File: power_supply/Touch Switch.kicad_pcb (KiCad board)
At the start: 2 copper layers, 82.9 x 49.8 mm, 51 parts, among them J1 Conn_01x01_Pin, J2 Conn_02x04_Counter_Clockwise, J3 Conn_01x01_Pin, J4 Conn_01x01_Pin, J5 Conn_01x01_Pin, J6 Conn_01x01_Pin, J7 Conn_01x01_Pin, J8 Conn_01x01_Pin, K1 Relay_SPST-NO, K2 Relay_SPST-NO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

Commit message: Modification : PCB
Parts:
- added G***: LOGO, LOGO, F.Cu at (191.8, 108.2)
- moved K2 8.88 mm to (191.2, 83.4)
- moved K4 8.78 mm to (204.9, 83.4)
- moved K3 8.77 mm to (177.6, 83.4)
- moved K1 8.72 mm to (218.5, 83.4)
- moved C6 1.45 mm to (150.4, 72.3), turned to 90 degrees
- moved D6 0.51 mm to (198.6, 77.9)
- moved Q1 0.51 mm to (194.9, 78.7)
- moved R12 0.51 mm to (191.8, 78.7)
- moved D5 0.35 mm to (225.9, 78.2)
- moved D7 0.10 mm to (212.7, 78.2)
- moved Q3 0.10 mm to (209.1, 79.0)
- moved R14 0.10 mm to (205.9, 79.0)
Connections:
- K1 pad 13: L -> R1
- K1 pad 14: R1 -> L
- K2 pad 13: L -> R3
- K2 pad 14: R3 -> L
- K3 pad 13: L -> R4
- K3 pad 14: R4 -> L
- K4 pad 13: L -> R2
- K4 pad 14: R2 -> L
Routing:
- net L: track 126.7 -> 0.00 mm, vias 46 -> 50
- net GND2: track 103.0 -> 199.2 mm, vias 4 -> 3
- net R1: track 23.7 -> 2.21 mm
- net R3: track 23.8 -> 2.28 mm
- net R2: track 23.8 -> 2.76 mm
- net R4: track 19.5 -> 0.01 mm
- net GND: track 59.2 -> 78.3 mm
- net N: track 23.2 -> 15.5 mm, vias 4 -> 6
- net Net-(D9-+): track 14.6 -> 21.0 mm, vias 0 -> 1
- net +5V: track 168.0 -> 163.3 mm
- net VCC_IC: track 8.73 -> 9.82 mm
- net Net-(D5-A): track 14.1 -> 13.1 mm
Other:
- board size 82.9 x 49.8 mm -> 82.9 x 50 mm

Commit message: Modified : PCB
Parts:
- moved R5 0.17 mm to (151.7, 69.8)
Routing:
- net Net-(S713XS1-FB): track 9.11 -> 3.58 mm, vias 2 -> 4
- net Prim: track 16.7 -> 11.5 mm, vias 3 -> 4
- net GND2: track 199.2 -> 195.7 mm, vias 3 -> 6
- net Net-(D9-+): track 21.0 -> 22.2 mm, vias 1 -> 2
- net GND: track 78.3 -> 79.1 mm, vias 3 -> 6

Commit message: Modified : PCB
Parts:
- moved R5 0.21 mm to (151.7, 69.5)
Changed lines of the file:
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@@
 	(footprint "Resistor_SMD:R_0805_2012Metric"
 		(layer "F.Cu")
-		(at 151.65 69.7625 180)
+		(at 151.65 69.55 180)
 		(descr "Resistor SMD 0805 (2012 Metric), square (rectangular) end terminal, IPC_7351 nominal, (Body size source: IPC-SM-782 page 72, https://www.pcb-3d.com/wordpress/wp-content/uploads/ipc-sm-782a_amendment_1_and_2.pdf), generated with kicad-footprint-generator")
 		(tags "resistor")
@@
 		(at 159.75 81.55)
 		(size 1)
-		(drill 0.25)
+		(drill 0.3)
 		(layers "F.Cu" "B.Cu")
 		(net 9)

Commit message: New Kicad Project + tree modified
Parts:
- moved R1 1.12 mm to (156.7, 95.1)
- moved L1 0.96 mm to (150.8, 97.1)
- moved C7 0.75 mm to (158.1, 102.2)
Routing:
- net GND: track 79.1 -> 83.3 mm
- net 310VDC: track 53.9 -> 56.1 mm
- net Net-(S713XS1-CS): track 1.93 -> 0.00 mm
- net Net-(C7-Pad1): track 7.92 -> 9.29 mm
- net Net-(D9-+): track 22.2 -> 23.6 mm
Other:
- board size 82.9 x 50 mm -> 84.5 x 50 mm

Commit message: PCB (control_card): Almost Finished
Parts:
- moved J2 5.21 mm to (220.9, 67.9)
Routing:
- net CT3: track 35.6 -> 30.8 mm
- net CT1: track 46.4 -> 41.8 mm
- net GND2: track 195.7 -> 192.1 mm
- net +3.3V: track 28.5 -> 24.9 mm
- net CT4: track 29.2 -> 27.5 mm
- net CT2: track 23.8 -> 22.5 mm
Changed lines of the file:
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@@
 	(footprint "Connector_PinSocket_2.54mm:PinSocket_2x04_P2.54mm_Vertical"
 		(layer "F.Cu")
-		(at 225.5 70.29 -90)
+		(at 220.895183 67.85825 -90)
 		(descr "Through hole straight socket strip, 2x04, 2.54mm pitch, double cols (from Kicad 4.0.7), script generated")
 		(tags "Through hole socket strip THT 2x04 2.54mm double row")
@@
 		(net 16)
 	)
+	(gr_line
+		(start 173.99 63.25)
+		(end 173.99 88.19)
+		(stroke
+			(width 0.1)
+			(type default)
+		)
+		(layer "Dwgs.User")
+	)
+	(gr_line
+		(start 173.99 88.19)
+		(end 229.58 88.19)
+		(stroke
+			(width 0.1)
+			(type default)
+		)
+		(layer "Dwgs.User")
+	)
 	(gr_arc
 		(start 173 80.5)
@@
 			(extension_offset 0.5) keep_text_aligned)
 	)
+	(dimension
+		(type aligned)
+		(layer "F.SilkS")
+		(pts
+			(xy 222.225183 63.98825) (xy 229.52 63.98)
+		)
+		(height -7.104325)
+		(gr_text "7,2948 mm"
+			(at 225.863313 55.779806 0.06479804972)
+			(layer "F.SilkS")
+			(effects
+				(font
+					(size 1 1)
+					(thickness 0.1)
+				)
+			)
+		)
+		(format
+			(prefix "")
+			(suffix "")
+			(units 3)
+			(units_format 1)
+			(precision 4)
+		)
+		(style
+			(thickness 0.1)
+			(arrow_length 1.27)
+			(text_position_mode 0)
+			(extension_height 0.58642)
+			(extension_offset 0.5) keep_text_aligned)
+	)
+	(dimension
+		(type aligned)
+		(layer "Dwgs.User")
+		(pts
+			(xy 173.99 63.25) (xy 229.52 63.25)
+		)
+		(height -13.01)
+		(gr_text "55,5300 mm"
+			(at 201.755 49.09 0)
+			(layer "Dwgs.User")
+			(effects
+				(font
+					(size 1 1)
+					(thickness 0.15)
+				)
+			)
+		)
+		(format
+			(prefix "")
+			(suffix "")
+			(units 3)
+			(units_format 1)
+			(precision 4)
+		)
+		(style
+			(thickness 0.1)
+			(arrow_length 1.27)
+			(text_position_mode 0)
+			(extension_height 0.58642)
+			(extension_offset 0.5) keep_text_aligned)
+	)
+	(dimension
+		(type aligned)
+		(layer "Dwgs.User")
+		(pts
+			(xy 229.52 63.25) (xy 229.58 88.19)
+		)
+		(height -16.153435)
+		(gr_text "24,9401 mm"
+			(at 246.853385 75.678372 270.1378404)
+			(layer "Dwgs.User")
+			(effects
+				(font
+					(size 1 1)
+					(thickness 0.15)
+				)
+			)
+		)
+		(format
+			(prefix "")
+			(suffix "")
+			(units 3)
+			(units_format 1)
+			(precision 4)
+		)
+		(style
+			(thickness 0.1)
+			(arrow_length 1.27)
+			(text_position_mode 0)
+			(extension_height 0.58642)
+			(extension_offset 0.5) keep_text_aligned)
+	)
 	(segment
 		(start 150.7 69.8)
@@
 	)
 	(segment
-		(start 205.925 77.9875)
-		(end 208.1375 77.9875)
+		(start 208.175 76.925)
+		(end 209.75 75.35)
 		(width 0.2)
 		(layer "F.Cu")
@@
 	)
 	(segment
-		(start 227 68.5)
-		(end 226.25 67.75)
+		(start 223.28 69.16)
+		(end 223.28 65.94)
 		(width 0.2)
 		(layer "F.Cu")
@@
 	)
 	(segment
-		(start 223.25 75.35)
-		(end 227 71.6)
+		(start 222.65825 65.31825)
+		(end 220.895183 65.31825)
 		(width 0.2)
 		(layer "F.Cu")
@@
 	)
 	(segment
-		(start 208.175 77.95)
-		(end 208.175 76.925)
+		(start 217.09 75.35)
+		(end 223.28 69.16)
 		(width 0.2)
 		(layer "F.Cu")
@@
 	)
 	(segment
-		(start 208.175 76.925)
-		(end 209.75 75.35)
+		(start 208.1375 77.9875)
+		(end 208.175 77.95)
 		(width 0.2)
 		(layer "F.Cu")
@@
 	)
 	(segment
-		(start 227 71.6)
-		(end 227 68.5)
+		(start 209.75 75.35)
+		(end 217.09 75.35)
 		(width 0.2)
 		(layer "F.Cu")
@@
 	)
 	(segment
-		(start 209.75 75.35)
-		(end 223.25 75.35)
+		(start 223.28 65.94)
+		(end 222.65825 65.31825)
 		(width 0.2)
 		(layer "F.Cu")
@@
 	)
 	(segment
-		(start 226.25 67.75)
-		(end 225.5 67.75)
+		(start 208.175 77.95)
+		(end 208.175 76.925)
 		(width 0.2)
 		(layer "F.Cu")
@@
 	)
 	(segment
-		(start 208.1375 77.9875)
-		(end 208.175 77.95)
+		(start 205.925 77.9875)
+		(end 208.1375 77.9875)
 		(width 0.2)
 		(layer "F.Cu")
@@
 	)
 	(segment
-		(start 222.96 72.24)
-		(end 220.45 74.75)
-		(width 0.2)
-		(layer "F.Cu")
-		(net 24)
-	)
-	(segment
-		(start 192.4125 77.8)
-		(end 192.3 77.6875)
+		(start 194.05 76.75)
+		(end 194.05 77.8)
 		(width 0.2)
 		(layer "F.Cu")
@@
 	)
 	(segment
-		(start 194.05 77.8)
-		(end 192.4125 77.8)
+		(start 196.05 74.75)
+		(end 194.05 76.75)
 		(width 0.2)
 		(layer "F.Cu")
@@
 	)
 	(segment
-		(start 220.45 74.75)
-		(end 196.05 74.75)
+		(start 218.355183 67.85825)
+		(end 211.463433 74.75)
 		(width 0.2)
 		(layer "F.Cu")
@@
 	)
 	(segment
-		(start 194.05 76.75)
-		(end 194.05 77.8)
+		(start 194.05 77.8)
+		(end 192.4125 77.8)
 		(width 0.2)
 		(layer "F.Cu")
@@
 	)
 	(segment
-		(start 222.96 70.29)
-		(end 222.96 72.24)
+		(start 192.4125 77.8)
+		(end 192.3 77.6875)
 		(width 0.2)
 		(layer "F.Cu")
@@
 	)
 	(segment
-		(start 196.05 74.75)
-		(end 194.05 76.75)
+		(start 211.463433 74.75)
+		(end 196.05 74.75)
 		(width 0.2)
 		(layer "F.Cu")
@@
 	)
 	(segment
+		(start 210.883433 70.25)
+		(end 213.275183 67.85825)
+		(width 1)
+		(layer "F.Cu")
+		(net 25)
+	)
+	(segment
 		(start 201.7 70.7)
 		(end 206.4375 70.7)
@@
 	)
 	(segment
-		(start 217.84 70.25)
-		(end 217.88 70.29)
-		(width 1)
-		(layer "F.Cu")
-		(net 25)
-	)
-	(segment
 		(start 189.55 78.75)
 		(end 190.3125 79.5125)
@@
 	)
 	(segment
-		(start 209 70.25)
-		(end 217.84 70.25)
-		(width 1)
-		(layer "F.Cu")
-		(net 25)
-	)
-	(segment
 		(start 185.2 70.3)
 		(end 188 73.1)
@@
 		(net 25)
 	)
+	(segment
+		(start 209 70.25)
+		(end 210.883433 70.25)
+		(width 1)
+		(layer "F.Cu")
+		(net 25)
+	)
 	(via
 		(at 189.55 77.95)
@@
 	)
 	(segment
-		(start 227.8 66.2)
-		(end 227.1 65.5)
+		(start 221.425 77.8875)
+		(end 221.4625 77.85)
 		(width 0.2)
 		(layer "F.Cu")
@@
 	)
 	(segment
-		(start 227.1 65.5)
-		(end 223.7 65.5)
+		(start 223.78 64.76)
+		(end 223.78 69.56)
 		(width 0.2)
 		(layer "F.Cu")
@@
 	)
 	(segment
-		(start 221.425 77.8875)
-		(end 221.4625 77.85)
+		(start 219.505183 64.16825)
+		(end 223.18825 64.16825)
 		(width 0.2)
 		(layer "F.Cu")
@@
 	)
 	(segment
-		(start 221.4625 77.85)
-		(end 222.05 77.85)
+		(start 221.4625 71.8775)
+		(end 221.4625 77.85)
 		(width 0.2)
 		(layer "F.Cu")
@@
 	)
 	(segment
-		(start 223.7 65.5)
-		(end 222.96 66.24)
+		(start 223.78 69.56)
+		(end 221.4625 71.8775)
 		(width 0.2)
 		(layer "F.Cu")
@@
 	)
 	(segment
-		(start 227.8 72.1)
-		(end 227.8 66.2)
+		(start 218.355183 65.31825)
+		(end 219.505183 64.16825)
 		(width 0.2)
 		(layer "F.Cu")
@@
 	)
 	(segment
-		(start 222.96 66.24)
-		(end 222.96 67.75)
+		(start 223.18825 64.16825)
+		(end 223.78 64.76)
 		(width 0.2)
 		(layer "F.Cu")
@@
 	)
 	(segment
-		(start 222.05 77.85)
-		(end 227.8 72.1)
-		(width 0.2)
-		(layer "F.Cu")
-		(net 26)
-	)
-	(segment
 		(start 181.125 77.65)
 		(end 181.125 76.0125)
@@
 	)
 	(segment
-		(start 182.9375 74.2)
-		(end 218.2 74.2)
+		(start 209.473433 74.2)
+		(end 215.815183 67.85825)
 		(width 0.2)
 		(layer "F.Cu")
@@
 	)
 	(segment
-		(start 220.42 71.98)
-		(end 220.42 70.29)
-		(width 0.2)
-		(layer "F.Cu")
-		(net 27)
-	)
-	(segment
 		(start 179.15 77.65)
 		(end 179.0625 77.7375)
@@
 	)
 	(segment
-		(start 218.2 74.2)
-		(end 220.42 71.98)
+		(start 182.9375 74.2)
+		(end 209.473433 74.2)
 		(width 0.2)
 		(layer "F.Cu")
@@
 	)
 	(segment
-		(start 217.28 68.35)
-		(end 217.88 67.75)
-		(width 1)
-		(layer "F.Cu")
-		(net 28)
-	)
-	(segment
 		(start 208.4875 67.8375)
 		(end 209 68.35)
@@
 	)
 	(segment
-		(start 209 68.35)
-		(end 217.28 68.35)
-		(width 1)
-		(layer "F.Cu")
-		(net 28)
-	)
-	(segment
 		(start 196.85 69.6)
 		(end 190.55 69.6)
@@
 	)
 	(segment
+		(start 210.243433 68.35)
+		(end 213.275183 65.31825)
+		(width 1)
+		(layer "F.Cu")
+		(net 28)
+	)
+	(segment
 		(start 196.85 69.6)
 		(end 198.7 69.6)
 		(width 1)
 		(layer "F.Cu")
+		(net 28)
+	)
+	(segment
+		(start 209 68.35)
+		(end 210.243433 68.35)
+		(width 1)
+		(layer "F.Cu")

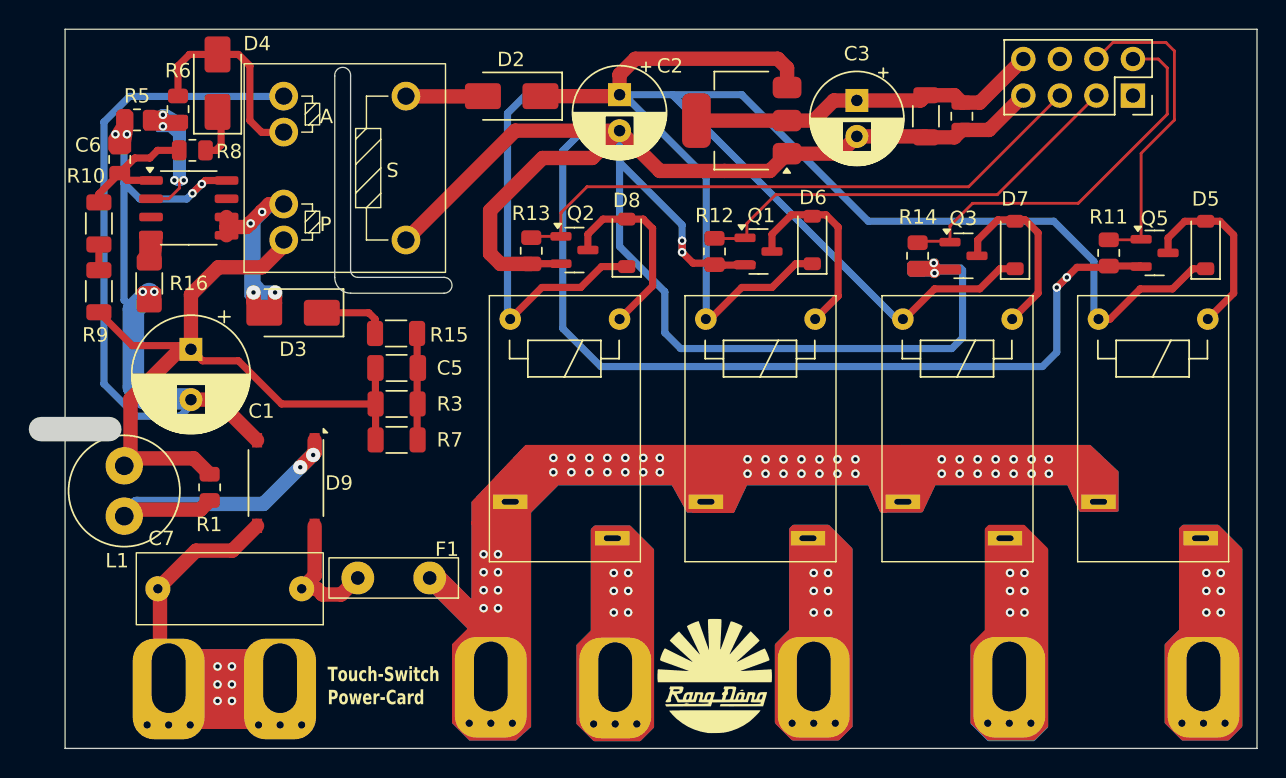
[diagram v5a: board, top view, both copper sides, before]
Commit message: PCB (control_card): V2 almost finished
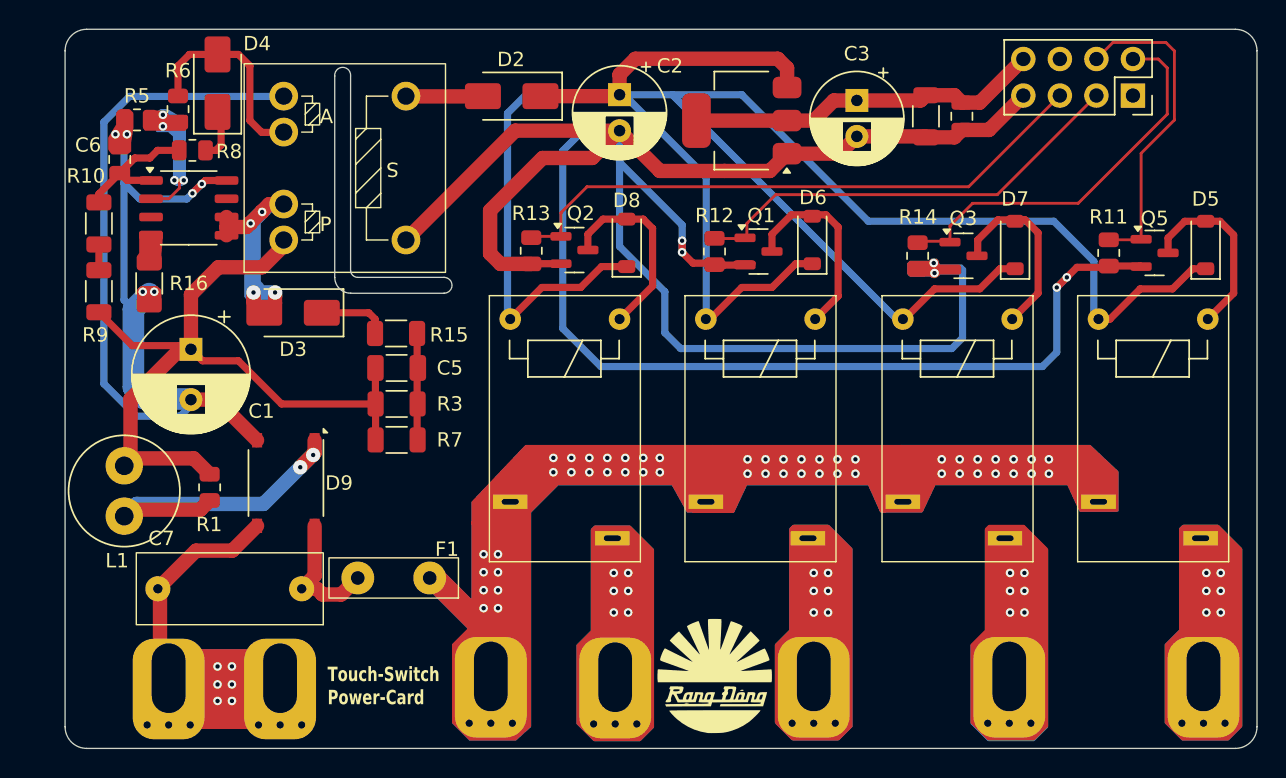
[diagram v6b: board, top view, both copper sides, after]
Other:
- board size 84.5 x 50 mm -> 82.9 x 50 mm
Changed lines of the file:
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@@
+	)
+	(gr_arc
+		(start 146.65 64.75)
+		(mid 147.08934 63.68934)
+		(end 148.15 63.25)
+		(stroke
+			(width 0.05)
+			(type default)
+		)
+		(layer "Edge.Cuts")
 	)
 	(gr_arc
@@
 	)
 	(gr_line
-		(start 144.975 91.05)
-		(end 149.725 91.05)
-		(stroke
-			(width 1.7)
-			(type default)
-		)
-		(layer "Edge.Cuts")
-	)
-	(gr_line
 		(start 166.5 66.5)
 		(end 166.5 80)
+		(stroke
+			(width 0.05)
+			(type default)
+		)
+		(layer "Edge.Cuts")
+	)
+	(gr_line
+		(start 146.65 111.75)
+		(end 146.65 64.75)
+		(stroke
+			(width 0.05)
+			(type default)
+		)
+		(layer "Edge.Cuts")
+	)
+	(gr_arc
+		(start 229.52 111.75)
+		(mid 229.08066 112.81066)
+		(end 228.02 113.25)
+		(stroke
+			(width 0.05)
+			(type default)
+		)
+		(layer "Edge.Cuts")
+	)
+	(gr_line
+		(start 148.15 63.25)
+		(end 228.02 63.25)
+		(stroke
+			(width 0.05)
+			(type default)
+		)
+		(layer "Edge.Cuts")
+	)
+	(gr_line
+		(start 228.02 113.25)
+		(end 148.15 113.25)
 		(stroke
 			(width 0.05)
@@
 		(layer "Edge.Cuts")
 	)
+	(gr_line
+		(start 229.52 64.75)
+		(end 229.52 111.75)
+		(stroke
+			(width 0.05)
+			(type default)
+		)
+		(layer "Edge.Cuts")
+	)
+	(gr_arc
+		(start 228.02 63.25)
+		(mid 229.08066 63.68934)
+		(end 229.52 64.75)
+		(stroke
+			(width 0.05)
+			(type default)
+		)
+		(layer "Edge.Cuts")
+	)
 	(gr_arc
 		(start 167 80.5)
@@
 		(layer "Edge.Cuts")
 	)
-	(gr_rect
-		(start 146.65 63.25)
-		(end 229.52 113.25)
-		(stroke
-			(width 0.05)
-			(type default)
-		)
-		(fill none)
-		(layer "Edge.Cuts")
-	)
 	(gr_arc
 		(start 166.5 81.6)
 		(mid 165.722183 81.277817)
 		(end 165.4 80.5)
+		(stroke
+			(width 0.05)
+			(type default)
+		)
+		(layer "Edge.Cuts")
+	)
+	(gr_arc
+		(start 148.15 113.25)
+		(mid 147.08934 112.81066)
+		(end 146.65 111.75)
 		(stroke
 			(width 0.05)
@@
 		(layer "F.SilkS")
 		(pts
-			(xy 222.225183 63.98825) (xy 229.52 63.98)
+			(xy 222.355183 63.10825) (xy 229.65 63.1)
 		)
 		(height -7.104325)
 		(gr_text "7,2948 mm"
-			(at 225.863313 55.779806 0.06479804972)
+			(at 225.993313 54.899806 0.06479804972)
 			(layer "F.SilkS")
 			(effects

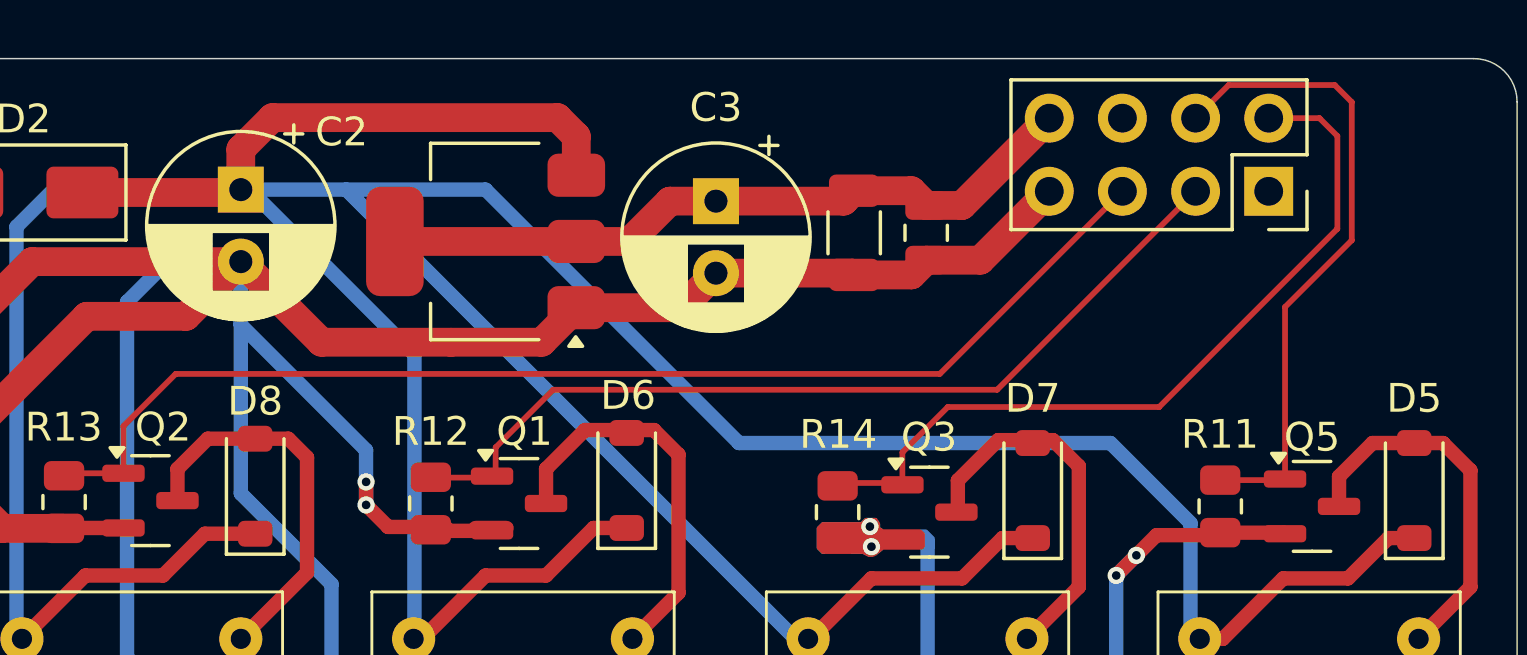
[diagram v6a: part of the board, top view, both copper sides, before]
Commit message: PCB (control_card) : V3 finished, perfect dimension
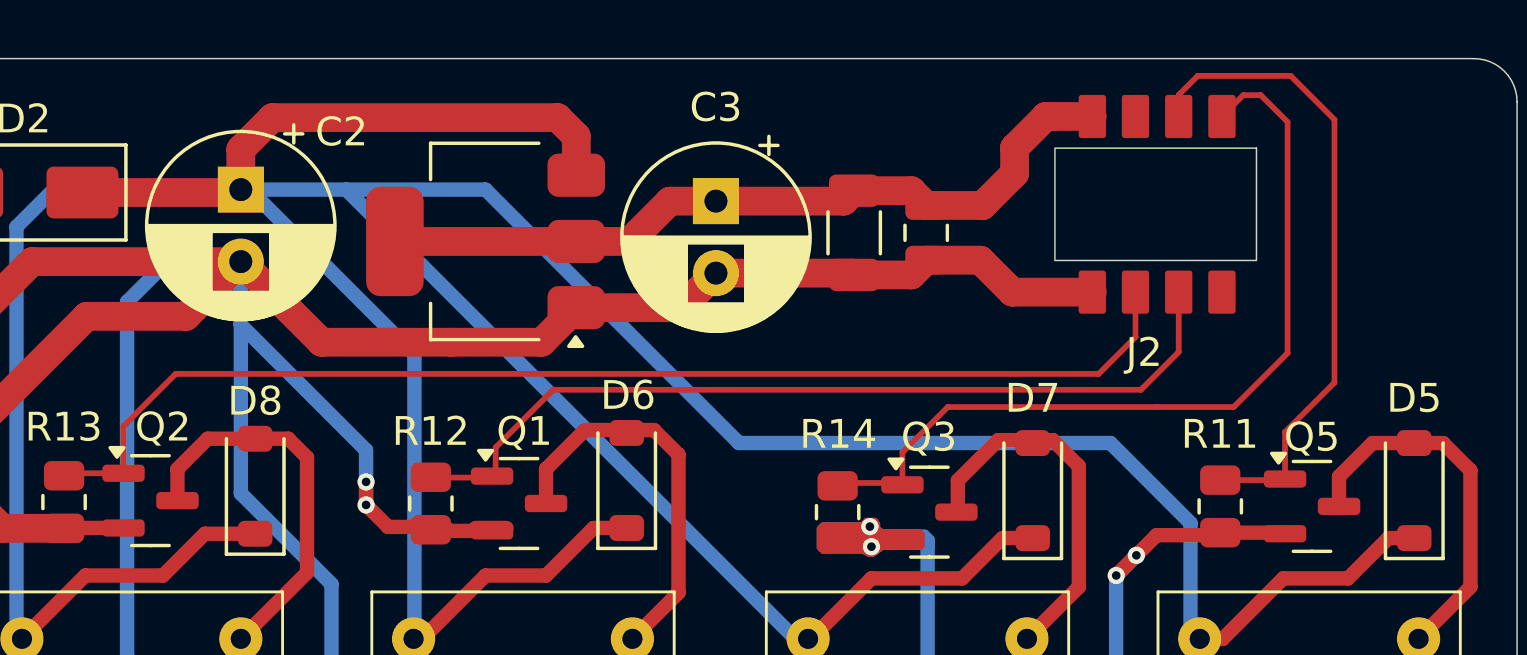
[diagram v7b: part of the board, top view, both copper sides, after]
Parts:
- J2: footprint Connector_PinSocket_2.54mm:PinSocket_2x04_P2.54mm_Vertical -> Footprint_Rang_Dong:Female connector
- moved J2 3.06 mm to (219.3, 65.3), turned to 180 degrees
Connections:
- J2 pad 1: unconnected-(J2-Pin_1-Pad1) -> CT4
- J2 pad 2: CT4 -> unconnected-(J2-Pin_2-Pad2)
- J2 pad 3: CT3 -> CT2
- J2 pad 4: CT2 -> CT3
- J2 pad 5: CT1 -> unconnected-(J2-Pin_5-Pad5)
- J2 pad 6: unconnected-(J2-Pin_6-Pad6) -> CT1
- J2 pad 7: GND2 -> +3.3V
- J2 pad 8: +3.3V -> GND2
- K1 pad 13: R1 -> L
- K1 pad 14: L -> R1
- K2 pad 13: R3 -> L
- K2 pad 14: L -> R3
- K3 pad 13: R4 -> L
- K3 pad 14: L -> R4
- K4 pad 13: R2 -> L
- K4 pad 14: L -> R2
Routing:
- net +3.3V: track 24.9 -> 27.2 mm
- net CT4: track 27.5 -> 29.2 mm
- net GND2: track 192.1 -> 193.0 mm
- net CT3: track 30.8 -> 30.0 mm
